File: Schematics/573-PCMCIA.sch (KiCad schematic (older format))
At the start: 2 parts

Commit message: Added GE675-PWB(A)
IO Board for Fisherman's Bait 3
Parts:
- gave numbers to parts that had none: 1
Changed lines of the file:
@@
 $EndDescr
 $Comp
-L Connectors_PC:FCN-565P136 C?
+L Connectors_PC:FCN-565P136 C39
 U 1 1 62CFBA62
 P 3550 3550
-F 0 "C?" H 3525 5965 50  0000 C CNN
+F 0 "C39" H 3525 5965 50  0000 C CNN
 F 1 "FCN-565P136" H 3525 5874 50  0000 C CNN
 F 2 "" H 4900 2250 50  0001 C CNN
@@
 $EndComp
 $Comp
-L power:+5V #PWR?
+L power:+5V #PWR0154
 U 1 1 62D02C9F
 P 2750 1200
-F 0 "#PWR?" H 2750 1050 50  0001 C CNN
+F 0 "#PWR0154" H 2750 1050 50  0001 C CNN
 F 1 "+5V" H 2765 1373 50  0000 C CNN
 F 2 "" H 2750 1200 50  0001 C CNN
@@
 $EndComp
 $Comp
-L power:GND #PWR?
+L power:GND #PWR0155
 U 1 1 62D040D2
 P 2750 5550
-F 0 "#PWR?" H 2750 5300 50  0001 C CNN
+F 0 "#PWR0155" H 2750 5300 50  0001 C CNN
 F 1 "GND" H 2755 5377 50  0000 C CNN
 F 2 "" H 2750 5550 50  0001 C CNN
@@
 NoConn ~ 2900 4850
 $Comp
-L Connectors_PC:FCN-565P136 C?
-U 1 1 62D9F529
+L Connectors_PC:FCN-565P136 C39
+U 2 1 62D9F529
 P 7400 3550
-F 0 "C?" H 7375 5965 50  0000 C CNN
+F 0 "C39" H 7375 5965 50  0000 C CNN
 F 1 "FCN-565P136" H 7375 5874 50  0000 C CNN
 F 2 "" H 8750 2250 50  0001 C CNN
 F 3 "" H 8750 2250 50  0001 C CNN
-	1    7400 3550
-	1    0    0    -1
-$EndComp
-$Comp
-L power:+5V #PWR?
+	2    7400 3550
+	1    0    0    -1
+$EndComp
+$Comp
+L power:+5V #PWR0156
 U 1 1 62D9F683
 P 6600 1200
-F 0 "#PWR?" H 6600 1050 50  0001 C CNN
+F 0 "#PWR0156" H 6600 1050 50  0001 C CNN
 F 1 "+5V" H 6615 1373 50  0000 C CNN
 F 2 "" H 6600 1200 50  0001 C CNN
@@
 $EndComp
 $Comp
-L power:GND #PWR?
+L power:GND #PWR0157
 U 1 1 62D9F68D
 P 6600 5550
-F 0 "#PWR?" H 6600 5300 50  0001 C CNN
+F 0 "#PWR0157" H 6600 5300 50  0001 C CNN
 F 1 "GND" H 6605 5377 50  0000 C CNN
 F 2 "" H 6600 5550 50  0001 C CNN

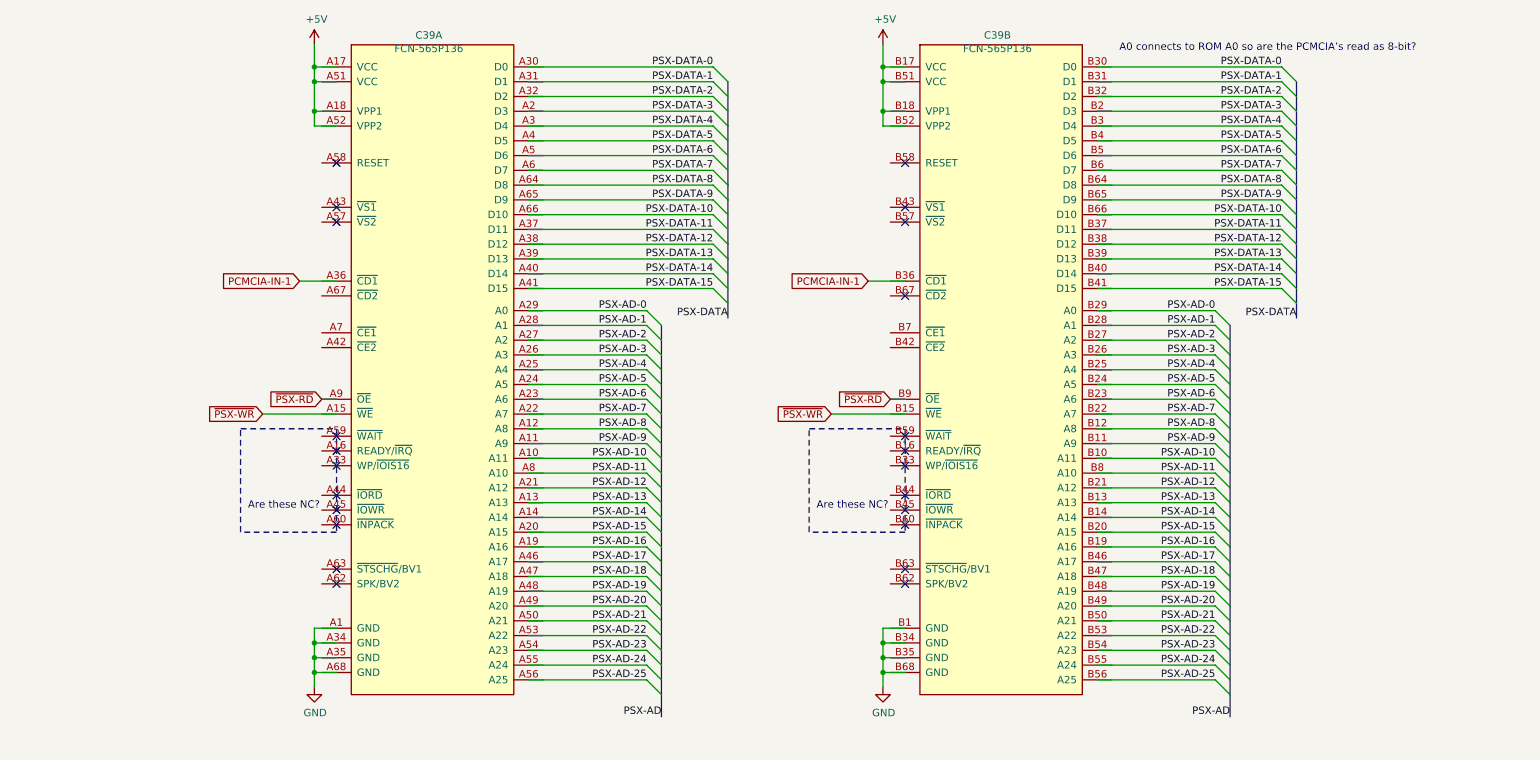
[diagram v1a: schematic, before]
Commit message: Updated Schematics
PCMCIA is pinned out
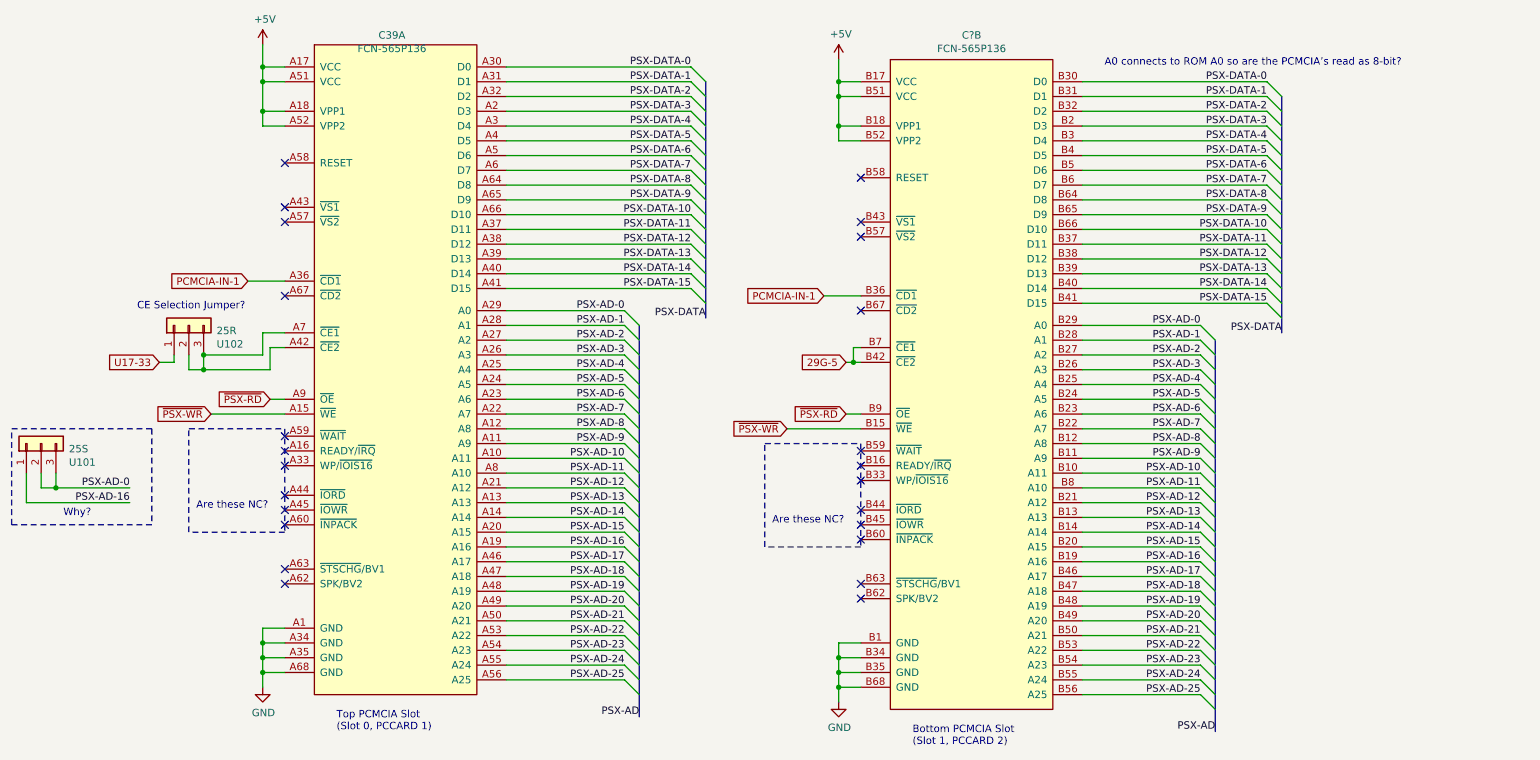
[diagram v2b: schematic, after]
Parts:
- removed unit 2 of C39
- added 25R: U102, Connector_PinHeader_2.54mm:PinHeader_1x03_P2.54mm_Vertical, symbol Connector_Generic:Conn_01x03
- added 25S: U101, Connector_PinHeader_2.54mm:PinHeader_1x03_P2.54mm_Vertical, symbol Connector_Generic:Conn_01x03
- added C?: FCN-565P136, symbol Connectors_PC:FCN-565P136
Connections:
- net labels added: 29G-5, U17-33
- wire segments 122 -> 143
- no-connect marks 23 -> 24
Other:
- note added: "Bottom PCMCIA Slot\n(Slot 1, PCCARD 2)"
- note added: "CE Selection Jumper?\n"
- note added: "Top PCMCIA Slot\n(Slot 0, PCCARD 1)"
- note added: "Why?"
- moved on the sheet: C39A
